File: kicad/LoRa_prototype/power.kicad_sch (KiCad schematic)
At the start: 51 parts, among them J10 SYS, J15 SYS, J2 USB_C_Receptacle_PowerOnly_6P, J3 BAT, J5 FG, U1 TC1262-33, U2 BQ24074RGTT, U3 MAX17048, U4 SPV1050

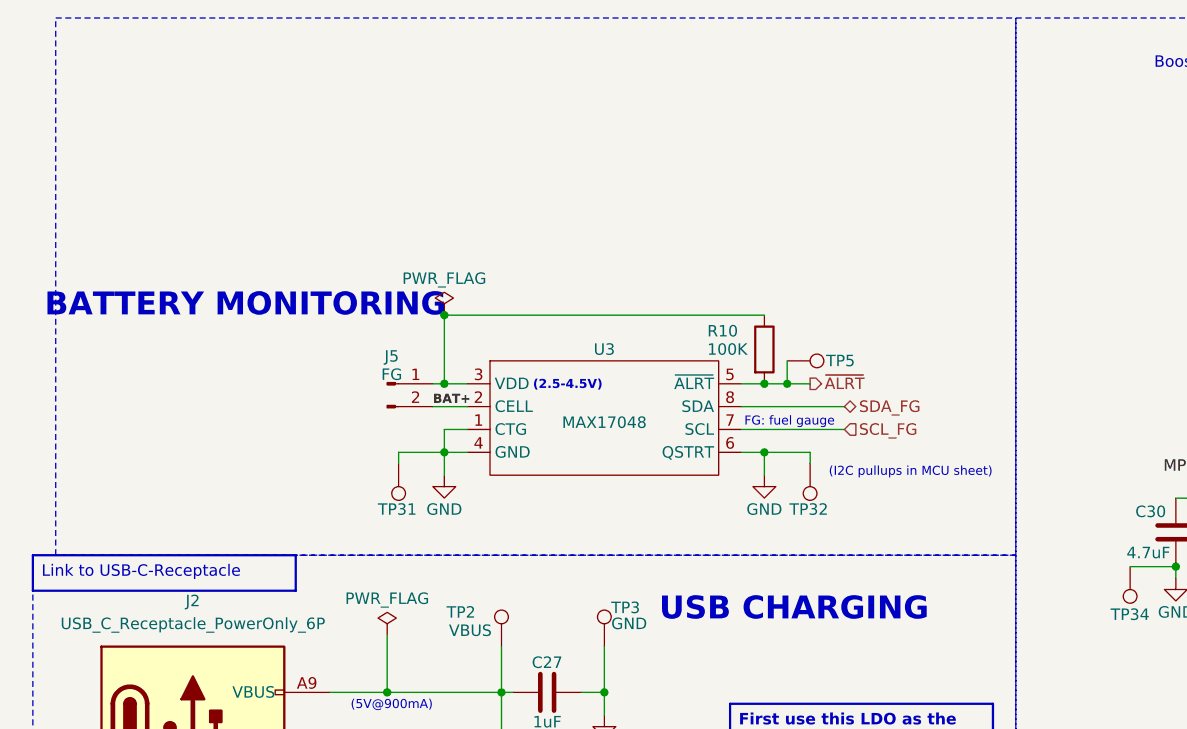
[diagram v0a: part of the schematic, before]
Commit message: Done routing fuel gauge
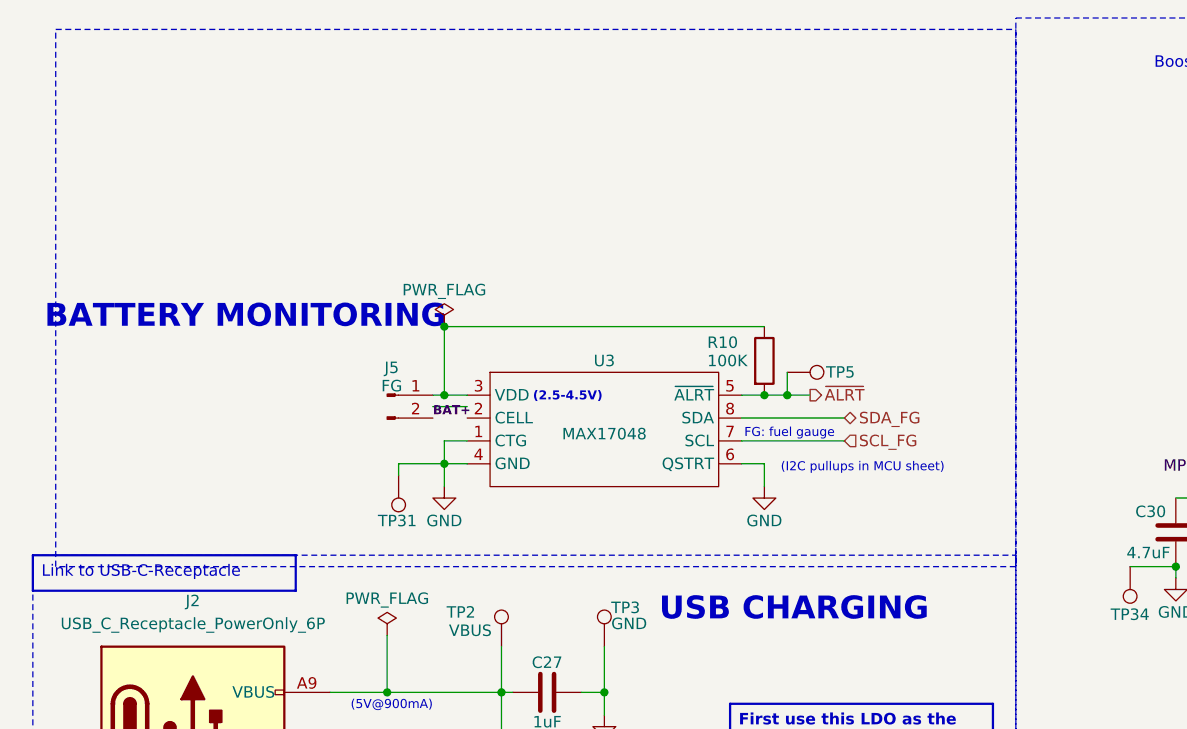
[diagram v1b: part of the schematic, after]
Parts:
- removed TP32: GND, TestPoint:TestPoint_Pad_2.0x2.0mm, symbol Connector:TestPoint
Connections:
- net BAT+: no longer U3.2 (CELL)
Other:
- moved on the sheet: J5, R10, TP31, TP5, U3

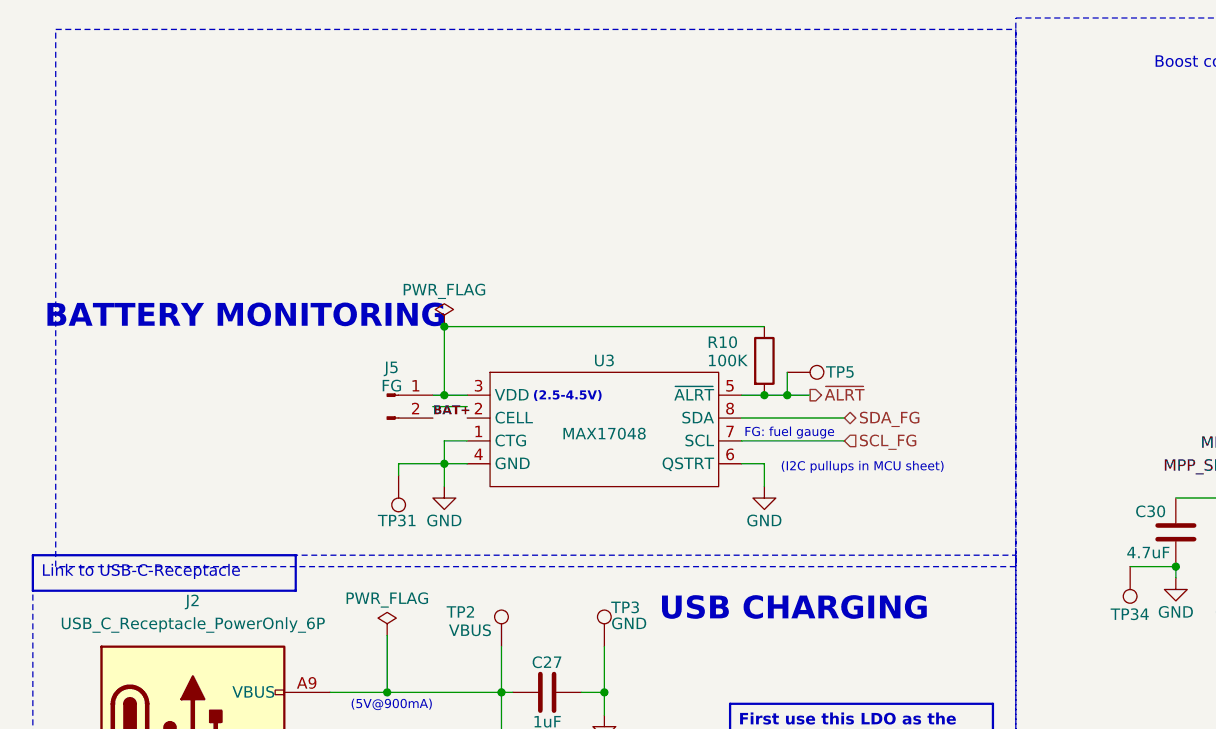
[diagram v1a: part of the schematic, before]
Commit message: Done routing gas sensors
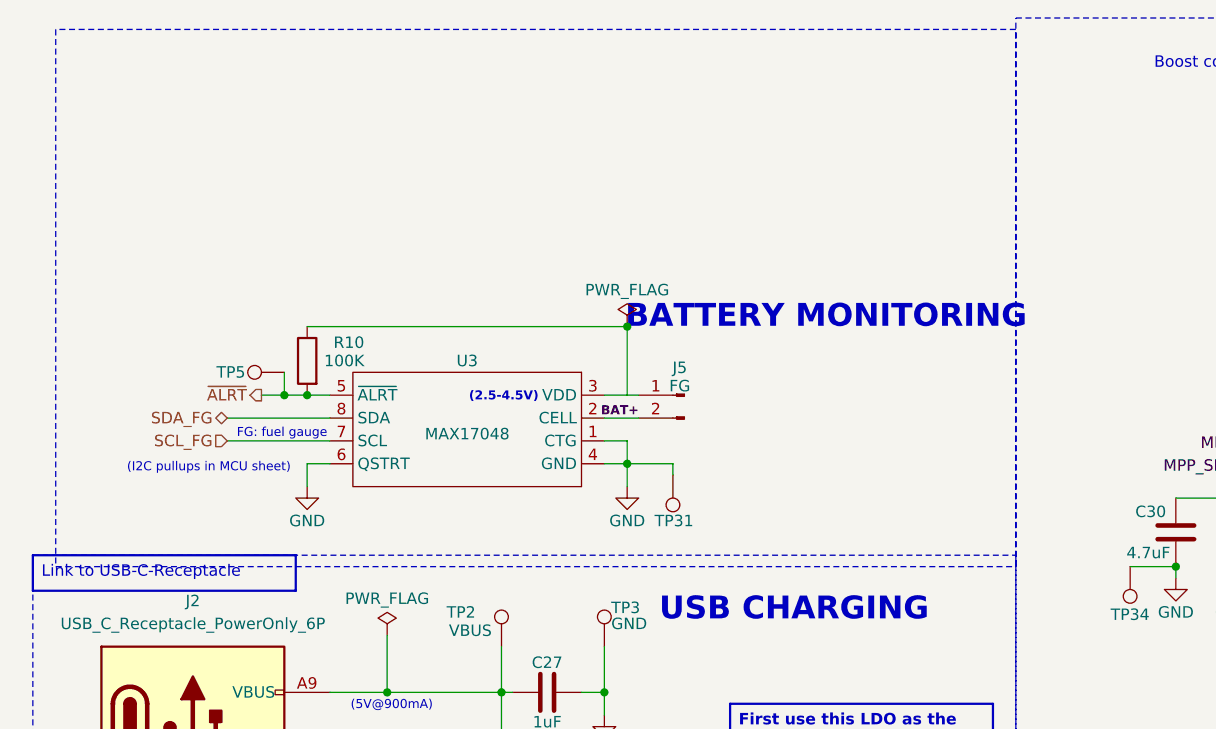
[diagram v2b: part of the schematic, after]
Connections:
- net BAT+: now also U3.2 (CELL)
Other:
- moved on the sheet: J5, R10, TP31, TP5, U3

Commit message: Changed decoupling in schematic
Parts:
- C27, C28, C29, C30, C32, C33, C34: footprint Capacitor_SMD:C_0805_2012Metric -> Capacitor_SMD:C_0603_1608Metric
- C31: footprint Capacitor_SMD:C_0805_2012Metric -> Capacitor_SMD:C_0402_1005Metric
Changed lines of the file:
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@@
 		(color 0 0 0 0)
 	)
+	(junction
+		(at 130.81 123.19)
+		(diameter 0)
+		(color 0 0 0 0)
+	)
 	(no_connect
 		(at 67.31 123.19)
@@
 	(wire
 		(pts
-			(xy 128.27 123.19) (xy 133.35 123.19)
+			(xy 128.27 123.19) (xy 130.81 123.19)
 		)
 		(stroke
@@
 	(wire
 		(pts
+			(xy 130.81 123.19) (xy 133.35 123.19)
+		)
+		(stroke
+			(width 0)
+			(type default)
+		)
+	)
+	(wire
+		(pts
 			(xy 209.55 111.76) (xy 212.09 111.76)
 		)
@@
 			)
 		)
-		(property "Footprint" "Capacitor_SMD:C_0805_2012Metric"
+		(property "Footprint" "Capacitor_SMD:C_0603_1608Metric"
 			(at 218.7448 34.29 0)
 			(hide yes)
@@
 			)
 		)
-		(property "Footprint" "Capacitor_SMD:C_0805_2012Metric"
+		(property "Footprint" "Capacitor_SMD:C_0603_1608Metric"
 			(at 227.6348 34.29 0)
 			(hide yes)
@@
 			)
 		)
-		(property "Footprint" "Capacitor_SMD:C_0805_2012Metric"
+		(property "Footprint" "Capacitor_SMD:C_0603_1608Metric"
 			(at 204.7748 87.63 0)
 			(hide yes)
@@
 			)
 		)
-		(property "Footprint" "Capacitor_SMD:C_0805_2012Metric"
+		(property "Footprint" "Capacitor_SMD:C_0603_1608Metric"
 			(at 94.2848 115.57 0)
 			(hide yes)
@@
 	)
 	(symbol
+		(lib_id "power:PWR_FLAG")
+		(at 130.81 123.19 180)
+		(unit 1)
+		(body_style 1)
+		(exclude_from_sim no)
+		(in_bom yes)
+		(on_board yes)
+		(in_pos_files yes)
+		(dnp no)
+		(property "Reference" "#FLG02"
+			(at 130.81 125.095 0)
+			(hide yes)
+			(show_name no)
+			(do_not_autoplace no)
+			(effects
+				(font
+					(size 1.27 1.27)
+				)
+			)
+		)
+		(property "Value" "PWR_FLAG"
+			(at 130.81 127 0)
+			(show_name no)
+			(do_not_autoplace no)
+			(effects
+				(font
+					(size 1.27 1.27)
+				)
+			)
+		)
+		(property "Footprint" ""
+			(at 130.81 123.19 0)
+			(hide yes)
+			(show_name no)
+			(do_not_autoplace no)
+			(effects
+				(font
+					(size 1.27 1.27)
+				)
+			)
+		)
+		(property "Datasheet" ""
+			(at 130.81 123.19 0)
+			(hide yes)
+			(show_name no)
+			(do_not_autoplace no)
+			(effects
+				(font
+					(size 1.27 1.27)
+				)
+			)
+		)
+		(property "Description" "Special symbol for telling ERC where power comes from"
+			(at 130.81 123.19 0)
+			(hide yes)
+			(show_name no)
+			(do_not_autoplace no)
+			(effects
+				(font
+					(size 1.27 1.27)
+				)
+			)
+		)
+		(pin "1"
+		)
+		(instances
+			(project "LoRa_prototype"
+				(path "/9fad4700-f514-47ad-821a-b4076ecc08de/5f290f36-0c09-4232-84b9-bfe06ad06aa2"
+					(reference "#FLG02")
+					(unit 1)
+				)
+			)
+		)
+	)
+	(symbol
 		(lib_id "Connector:Conn_01x02_Pin")
 		(at 100.33 59.69 0)
@@
 			)
 		)
-		(property "Footprint" "Capacitor_SMD:C_0805_2012Metric"
+		(property "Footprint" "Capacitor_SMD:C_0603_1608Metric"
 			(at 106.9848 130.81 0)
 			(hide yes)
@@
 			)
 		)
-		(property "Footprint" "Capacitor_SMD:C_0805_2012Metric"
+		(property "Footprint" "Capacitor_SMD:C_0603_1608Metric"
 			(at 153.9748 71.12 0)
 			(hide yes)
@@
 			)
 		)
-		(property "Footprint" "Capacitor_SMD:C_0805_2012Metric"
+		(property "Footprint" "Capacitor_SMD:C_0402_1005Metric"
 			(at 201.6252 81.28 0)
 			(hide yes)
@@
 			)
 		)
-		(property "Footprint" "Capacitor_SMD:C_0805_2012Metric"
+		(property "Footprint" "Capacitor_SMD:C_0603_1608Metric"
 			(at 88.9 91.7448 0)
 			(hide yes)

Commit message: 90% done (before ground and power pour)
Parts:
- added TP6: ~{BATT_CONN}, TestPoint:TestPoint_Pad_2.0x2.0mm, symbol Connector:TestPoint
- added TP7: ~{BATT_CHG}, TestPoint:TestPoint_Pad_2.0x2.0mm, symbol Connector:TestPoint
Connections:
- net ~{BATT_CHG}: now also TP7.1
- net ~{BATT_CONN}: now also TP6.1

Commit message: Prettified silkscreen layer
0 errors and 33 warnings in DRC
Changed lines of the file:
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@@
 		(property "Value" "IN_LV"
 			(at 191.77 52.0699 90)
-			(show_name no)
+			(show_name yes)
 			(do_not_autoplace no)
 			(effects

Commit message: BOM consolidation
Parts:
- C32: footprint Capacitor_SMD:C_0603_1608Metric -> Capacitor_SMD:C_0805_2012Metric
- R11, R12: value 10M -> 1M
- R13: value 6.2M -> 1M
- R14: value 500K -> 82K; footprint Resistor_SMD:R_0805_2012Metric -> Resistor_SMD:R_0603_1608Metric
- R15: value 2.7M -> 470K
- R17: value 1.5M -> 200K
- R18: value 8.2M -> 1M
- R4: value 1.8K -> 2K
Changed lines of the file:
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@@
 			)
 		)
-		(property "Value" "500K"
+		(property "Value" "82K"
 			(at 213.106 107.442 0)
 			(show_name no)
@@
 			)
 		)
-		(property "Footprint" "Resistor_SMD:R_0805_2012Metric"
+		(property "Footprint" "Resistor_SMD:R_0603_1608Metric"
 			(at 210.312 106.68 90)
 			(hide yes)
@@
 			)
 		)
-		(property "Value" "10M"
+		(property "Value" "1M"
 			(at 162.306 120.142 0)
 			(show_name no)
@@
 			)
 		)
-		(property "Value" "8.2M"
+		(property "Value" "1M"
 			(at 237.236 52.832 0)
 			(show_name no)
@@
 			)
 		)
-		(property "Value" "10M"
+		(property "Value" "1M"
 			(at 154.686 120.142 0)
 			(show_name no)
@@
 			)
 		)
-		(property "Footprint" "Capacitor_SMD:C_0603_1608Metric"
+		(property "Footprint" "Capacitor_SMD:C_0805_2012Metric"
 			(at 204.7748 87.63 0)
 			(hide yes)
@@
 			)
 		)
-		(property "Value" "6.2M"
+		(property "Value" "1M"
 			(at 213.106 97.282 0)
 			(show_name no)
@@
 		(dnp no)
 		(property "Reference" "R5"
-			(at 56.642 145.796 90)
+			(at 57.15 145.542 90)
 			(show_name no)
 			(do_not_autoplace no)
@@
 		)
 		(property "Value" "1K"
-			(at 57.15 147.828 90)
+			(at 57.15 143.51 90)
 			(show_name no)
 			(do_not_autoplace no)
@@
 		(dnp no)
 		(property "Reference" "R4"
-			(at 59.944 138.938 90)
+			(at 59.69 138.938 90)
 			(show_name no)
 			(do_not_autoplace no)
@@
 			)
 		)
-		(property "Value" "1.8K"
-			(at 66.294 139.7 90)
+		(property "Value" "2K"
+			(at 59.69 140.97 90)
 			(show_name no)
 			(do_not_autoplace no)
@@
 			)
 		)
-		(property "Value" "1.5M"
+		(property "Value" "200K"
 			(at 237.236 45.212 0)
 			(show_name no)
@@
 			)
 		)
-		(property "Value" "2.7M"
+		(property "Value" "470K"
 			(at 213.106 117.602 0)
 			(show_name no)

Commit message: Changed L7 to power inductor
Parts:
- L7: footprint Inductor_SMD:L_0402_1005Metric -> footprints:PSPMAA0402-220M-ANP
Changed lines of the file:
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@@
 			)
 		)
-		(property "Footprint" "Inductor_SMD:L_0402_1005Metric"
+		(property "Footprint" "footprints:PSPMAA0402-220M-ANP"
 			(at 186.69 44.45 0)
 			(hide yes)

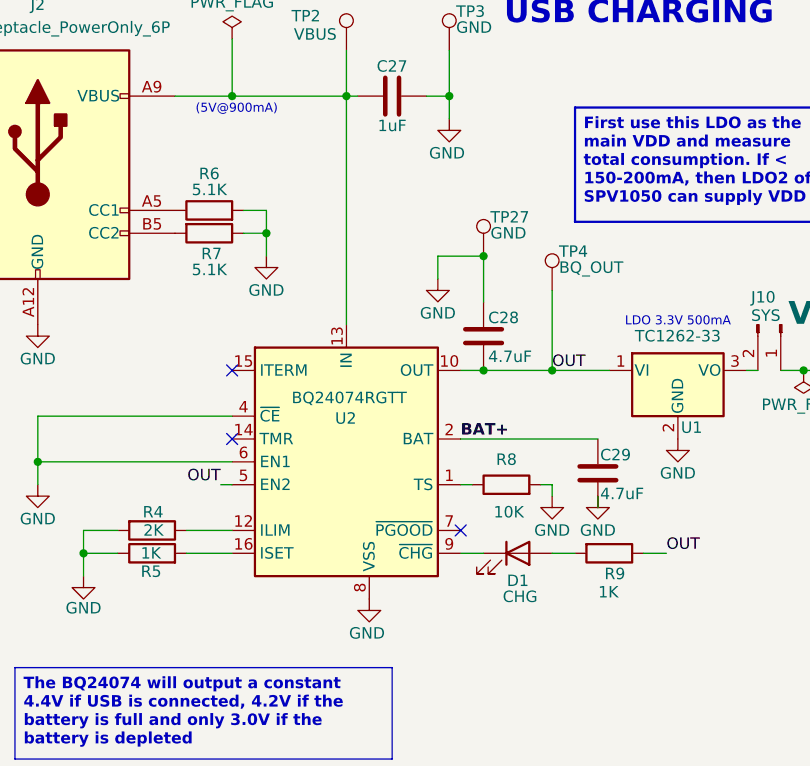
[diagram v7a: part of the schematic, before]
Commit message: Replaced DTC143ZEBTL with basic parts
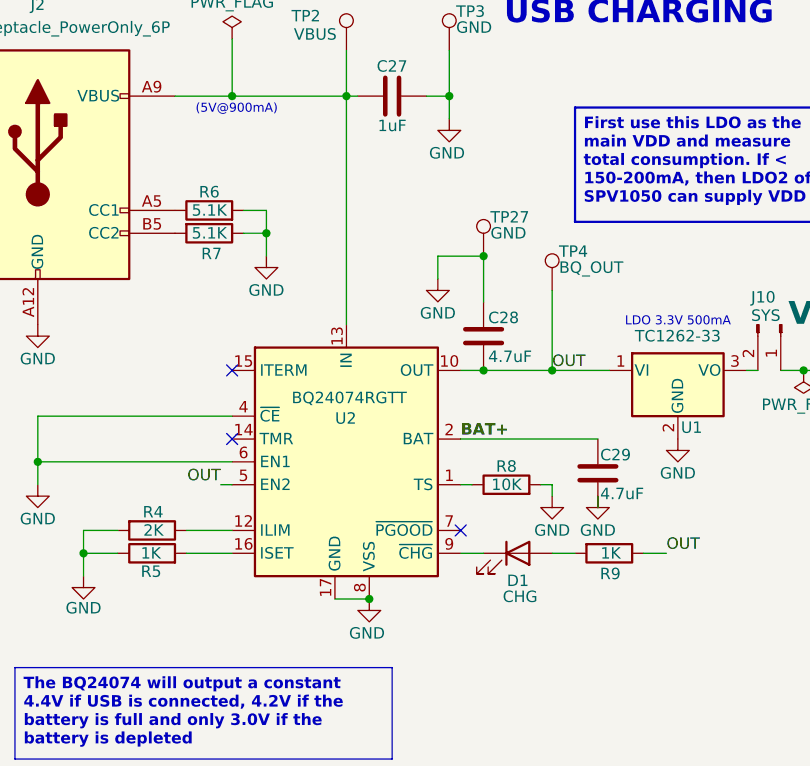
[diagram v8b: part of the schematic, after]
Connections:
- net GND: now also U2.17 (GND)
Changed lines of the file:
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@@
 	)
 	(junction
+		(at 82.55 148.59)
+		(diameter 0)
+		(color 0 0 0 0)
+	)
+	(junction
 		(at 154.94 78.74)
 		(diameter 0)
@@
 	(wire
 		(pts
+			(xy 78.74 148.59) (xy 82.55 148.59)
+		)
+		(stroke
+			(width 0)
+			(type default)
+		)
+	)
+	(wire
+		(pts
 			(xy 50.8 140.97) (xy 50.8 143.51)
 		)
@@
 		)
 		(property "Value" "5.1K"
-			(at 64.77 112.014 90)
+			(at 64.77 107.95 90)
 			(show_name no)
 			(do_not_autoplace no)
@@
 		(dnp no)
 		(property "Reference" "R6"
-			(at 64.77 101.346 90)
+			(at 64.77 103.378 90)
 			(show_name no)
 			(do_not_autoplace no)
@@
 		)
 		(property "Value" "5.1K"
-			(at 64.77 103.124 90)
+			(at 64.77 105.41 90)
 			(show_name no)
 			(do_not_autoplace no)
@@
 		(pin "9"
 		)
+		(pin "17"
+		)
 		(instances
 			(project "LoRa_prototype"
@@
 		(dnp no)
 		(property "Reference" "R9"
-			(at 110.998 145.796 90)
+			(at 110.49 145.796 90)
 			(show_name no)
 			(do_not_autoplace no)
@@
 		)
 		(property "Value" "1K"
-			(at 110.236 147.828 90)
+			(at 110.49 143.51 90)
 			(show_name no)
 			(do_not_autoplace no)
@@
 		(dnp no)
 		(property "Reference" "R8"
-			(at 97.79 133.096 90)
+			(at 97.79 133.858 90)
 			(show_name no)
 			(do_not_autoplace no)
@@
 		)
 		(property "Value" "10K"
-			(at 98.044 138.938 90)
+			(at 97.79 135.89 90)
 			(show_name no)
 			(do_not_autoplace no)
@@
 			"7542a80e-1430-4bb9-bab3-85b6fe3095be" "7620715f-3375-4a3d-9441-7319932c6382"
 			"76b839ee-4e0f-444f-a1be-78e2430f7b36" "76c65e56-74f1-40f5-a7bf-41e078eadd54"
-			"78aaf46f-9683-43b3-9a98-cbb41681b069" "7fc990f3-bb4f-4095-9fb3-168282f4b87e"
-			"8046a3dc-4d69-4e2b-9aa3-6ff30fa7aa3e" "834cd685-4171-4244-be6e-491b98c94e41"
-			"83da20ae-67d6-43de-b627-844aea8b773e" "85f24198-cd4e-4331-b449-3b0d30a5a4d1"
-			"868a5829-1a6e-4a2a-acea-dc354bd9375e" "87b47428-485f-49f1-9e98-f1a5620a7f27"
-			"895f76b3-dfa7-474a-915b-7c14e7be5d31" "8a08cdc5-0da8-4fb2-b7dc-b38bb792e6a4"
-			"8ad8f97c-d121-49ae-a8eb-66ee61dc3e9b" "8eb2b09e-806c-4948-b1b2-e00f1869fe03"
-			"91c81378-1589-432e-85fc-fd990777d213" "92461dfe-7dc1-459a-8e09-c0f3ef9803b2"
-			"94471df4-0c86-4a05-b588-ea002a67924d" "9541b335-7832-4153-ad49-c45b8932b985"
-			"97965d07-c9ec-43be-8c8f-e2033080df90" "9a329e44-bfa3-4818-8812-29979b08276b"
-			"9de5a1e5-ee28-402d-9dd7-2d45dc0d8024" "a8614e4f-d325-494f-af6e-e0da983fd2ea"
-			"aa2cba69-aec2-4bc9-9406-a6f3da0db1fe" "ae3053b4-115e-4b76-81b0-fbaeb94f27db"
-			"b336cc52-ea98-402f-853d-335fef28a859" "b39546db-1915-49ef-9aac-c7958663adae"
-			"b98d5f9d-7db8-43d9-8e62-da5b473400b5" "bd0d8184-9210-4ccf-b78c-09f32b56abc3"
-			"be3c6c0a-f50d-4a35-b392-eb562d24de30" "c219d99f-51ff-4033-bd79-8b2f6d5ff907"
-			"c369d34f-0279-43f7-8e62-d515ee5e137c" "c38673ba-d9f6-472a-a589-ec366962bbc1"
-			"c523b646-58af-4ac2-b96d-eb1f52ed2117" "c73048a0-de71-4700-a146-66fbedba28af"
-			"c769fe5f-971b-4b6e-95b5-3d3dc5ee5efa" "d1fda7c0-454d-49d3-b614-9e0d56f116ff"
-			"d6f28cbb-6360-4f1c-83dc-4e461ab27154" "d9cbc6dc-f403-4a5e-b66f-e6647fd9c796"
-			"dc3e67fe-721c-4dfd-be6d-d15449b3e772" "dcdd15e4-8fcb-4eb8-b2e1-62857ae4dece"
-			"e30c373b-a4d6-4257-84f3-d39e5cda2d30" "e3d2cb0b-7666-440e-bb43-34a346acf2d3"
-			"e4fc5512-e473-4f3c-a370-db67866444e2" "e89ab80b-d04d-4dd5-a74e-e66792c26431"
-			"ea2631b9-d313-4bcb-99d5-0f3f7e98a5ca" "eb7ab00c-10d9-4953-8834-33fb20c0eefb"
-			"f3bf8ef2-4591-4590-bcc4-122cb2412a2f" "f3c84562-ee03-4509-ba8b-3518a36ea5cf"
+			"78aaf46f-9683-43b3-9a98-cbb41681b069" "7cc99e24-54c3-44ea-b109-f946da52687d"
+			"7fc990f3-bb4f-4095-9fb3-168282f4b87e" "8046a3dc-4d69-4e2b-9aa3-6ff30fa7aa3e"
+			"834cd685-4171-4244-be6e-491b98c94e41" "83da20ae-67d6-43de-b627-844aea8b773e"
+			"85f24198-cd4e-4331-b449-3b0d30a5a4d1" "868a5829-1a6e-4a2a-acea-dc354bd9375e"
+			"87b47428-485f-49f1-9e98-f1a5620a7f27" "895f76b3-dfa7-474a-915b-7c14e7be5d31"
+			"8a08cdc5-0da8-4fb2-b7dc-b38bb792e6a4" "8ad8f97c-d121-49ae-a8eb-66ee61dc3e9b"
+			"8eb2b09e-806c-4948-b1b2-e00f1869fe03" "91c81378-1589-432e-85fc-fd990777d213"
+			"92461dfe-7dc1-459a-8e09-c0f3ef9803b2" "94471df4-0c86-4a05-b588-ea002a67924d"
+			"9541b335-7832-4153-ad49-c45b8932b985" "97965d07-c9ec-43be-8c8f-e2033080df90"
+			"9a329e44-bfa3-4818-8812-29979b08276b" "9de5a1e5-ee28-402d-9dd7-2d45dc0d8024"
+			"a8614e4f-d325-494f-af6e-e0da983fd2ea" "aa2cba69-aec2-4bc9-9406-a6f3da0db1fe"
+			"ae3053b4-115e-4b76-81b0-fbaeb94f27db" "b336cc52-ea98-402f-853d-335fef28a859"
+			"b39546db-1915-49ef-9aac-c7958663adae" "b98d5f9d-7db8-43d9-8e62-da5b473400b5"
+			"bd0d8184-9210-4ccf-b78c-09f32b56abc3" "be3c6c0a-f50d-4a35-b392-eb562d24de30"
+			"c219d99f-51ff-4033-bd79-8b2f6d5ff907" "c369d34f-0279-43f7-8e62-d515ee5e137c"
+			"c38673ba-d9f6-472a-a589-ec366962bbc1" "c523b646-58af-4ac2-b96d-eb1f52ed2117"
+			"c73048a0-de71-4700-a146-66fbedba28af" "c769fe5f-971b-4b6e-95b5-3d3dc5ee5efa"
+			"d1fda7c0-454d-49d3-b614-9e0d56f116ff" "d6f28cbb-6360-4f1c-83dc-4e461ab27154"
+			"d9cbc6dc-f403-4a5e-b66f-e6647fd9c796" "dc3e67fe-721c-4dfd-be6d-d15449b3e772"
+			"dcdd15e4-8fcb-4eb8-b2e1-62857ae4dece" "e30c373b-a4d6-4257-84f3-d39e5cda2d30"
+			"e3d2cb0b-7666-440e-bb43-34a346acf2d3" "e4fc5512-e473-4f3c-a370-db67866444e2"
+			"e89ab80b-d04d-4dd5-a74e-e66792c26431" "ea2631b9-d313-4bcb-99d5-0f3f7e98a5ca"
+			"eb7ab00c-10d9-4953-8834-33fb20c0eefb" "f3bf8ef2-4591-4590-bcc4-122cb2412a2f"
+			"f3c84562-ee03-4509-ba8b-3518a36ea5cf" "f79ea9d6-e8b6-4ed2-b36b-42dec7c903b4"
 			"f7a09951-235a-407c-a18a-952f9c38c4d9" "fbce87b8-7507-4f0d-b9b1-3d1e4709bbe9"
 		)
